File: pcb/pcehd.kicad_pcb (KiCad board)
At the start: 2 copper layers, 118.2 x 73 mm, 163 parts, among them J1 HDMI_CONN, J2 Micro_SD_Card, P1 JTAG_CONN, Q1 BC847, Q2 BC847, U1 AP7361, U10 SN74LVCC4245APW, U11 SN74LVCC4245APW, U12 10CL025YE144C8N, U13 IS25LP016D-JBLE, U14 SN74LVCC4245APW, U15 TLV70012, U16 TLV70025, U17 TLV70012, U18 SN74LVCC4245APW, U19 SN74LVCC4245APW, U2 ADV7513, U20 SN74LVC2G17, U3 TLV70018, U4 PCEngineExpansion, U5 FS7140-01G-XTD, U6 PCM1808PWR, U7 SI5351C-B, U8 74153, U9 SN74LVCC4245APW, Y1 25.000MHz

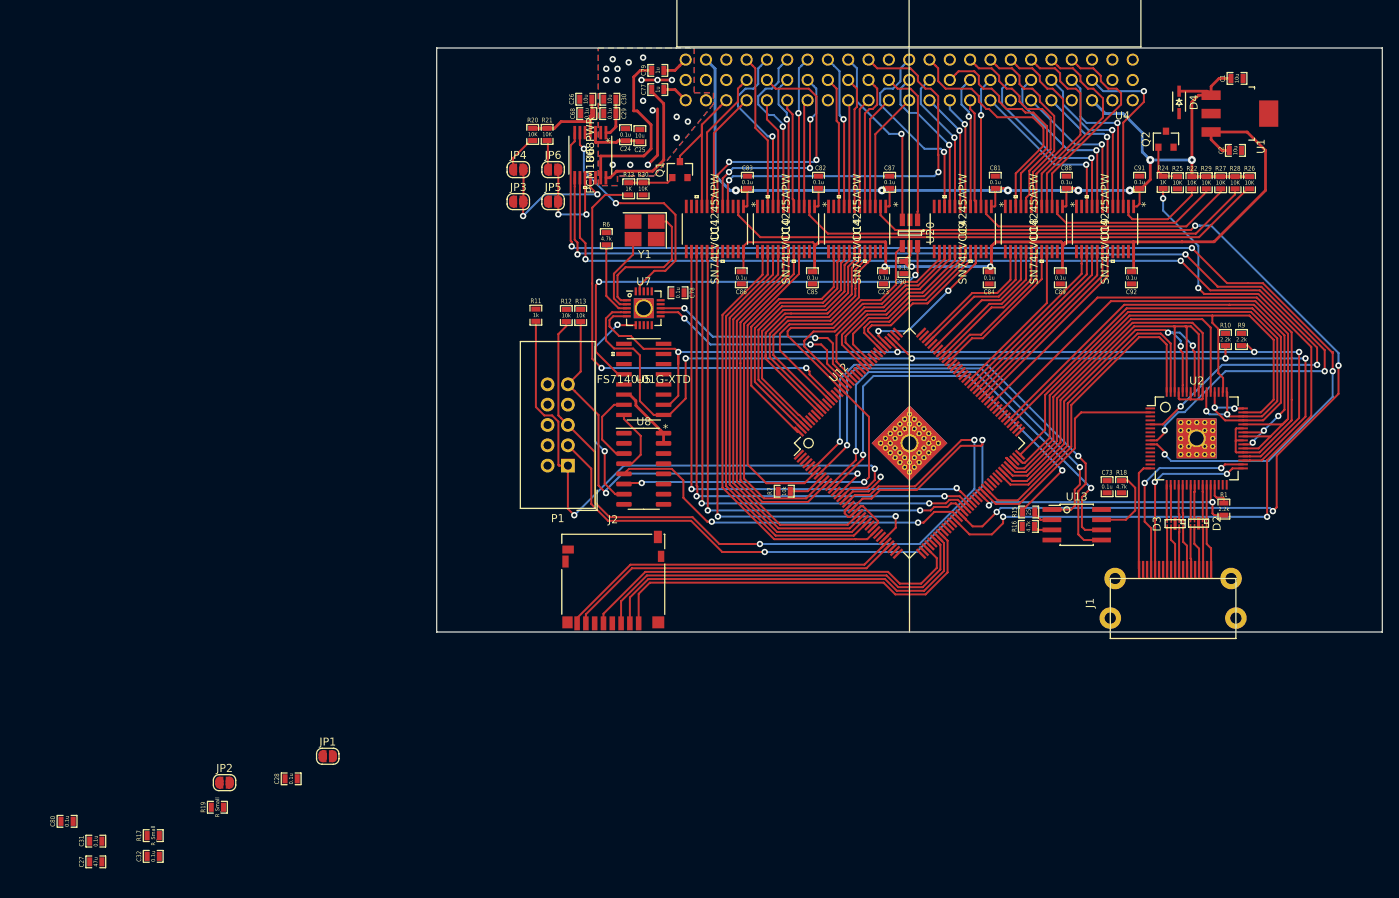
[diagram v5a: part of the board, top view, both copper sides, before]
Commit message: Removed unneeded jumpers
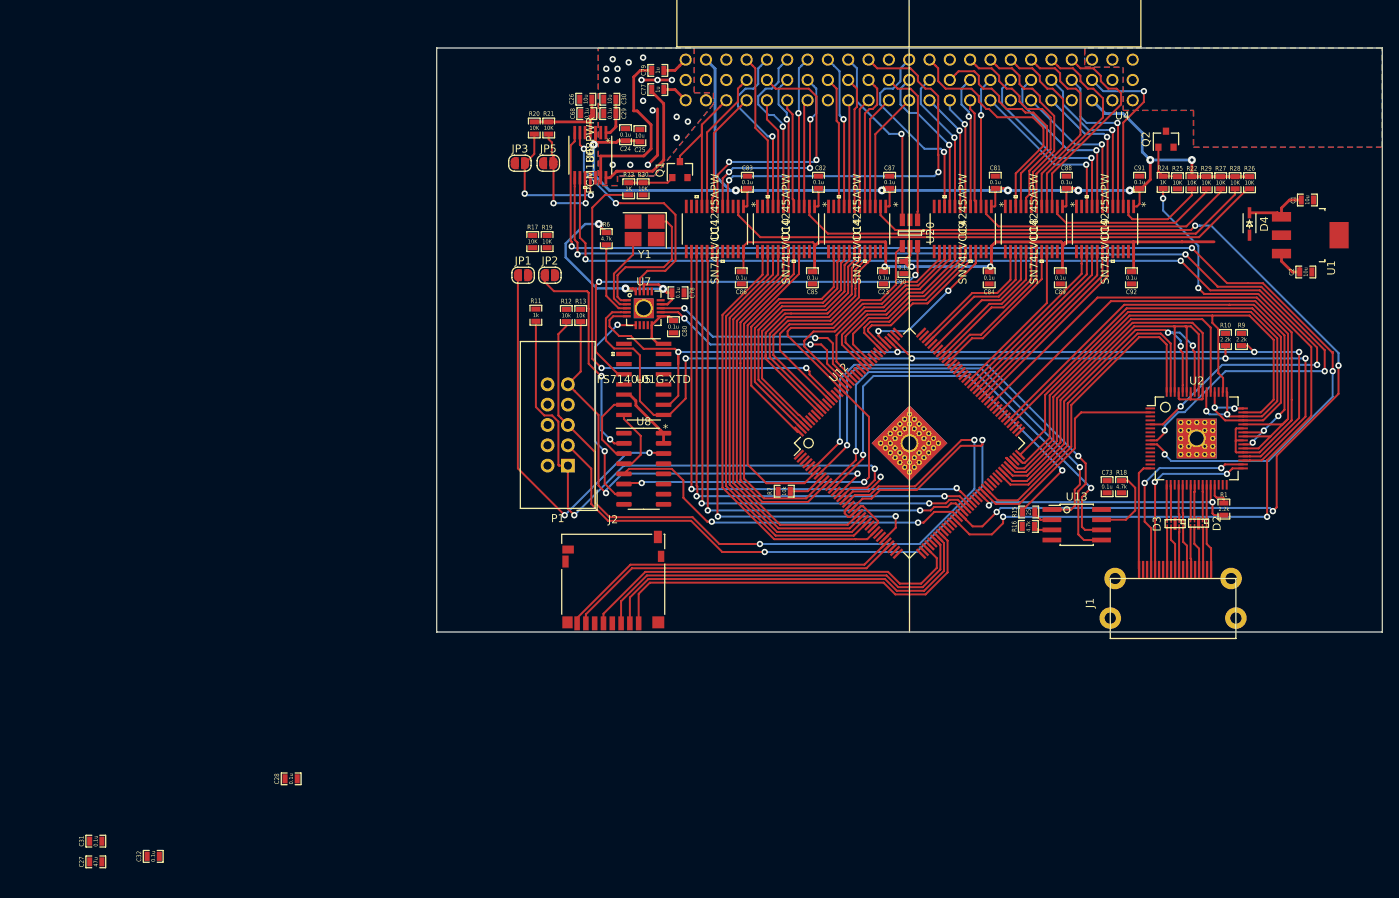
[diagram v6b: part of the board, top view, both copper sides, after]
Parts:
- removed JP4, JP6: SolderJumper_2_Open, Jumper:SolderJumper-2_P1.3mm_Open_RoundedPad1.0x1.5mm
- R17, R19: value R_Small -> 10K
- moved C80 97.8 mm to (101.0, 67.8), turned to 90 degrees
- moved R17 88.1 mm to (83.4, 57.2), turned to 90 degrees
- moved R19 81.8 mm to (85.2, 57.2), turned to 270 degrees
- moved JP2 75.3 mm to (85.5, 61.4)
- moved JP1 64.9 mm to (82.2, 61.4)
- moved C1 17.6 mm to (180.2, 52.0)
- moved C2 17.6 mm to (180.0, 61.0)
- moved D4 17.6 mm to (173.0, 55.0)
- moved U1 17.6 mm to (180.6, 56.4)
- moved JP5 4.84 mm to (85.3, 47.4)
- moved JP3 4.80 mm to (81.8, 47.4)
- moved R21 0.82 mm to (85.4, 43.0)
- moved R20 0.82 mm to (83.6, 43.0)
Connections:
- R20 pad 2: Net-(JP4-Pad1) -> Net-(JP3-Pad2)
- R21 pad 2: Net-(JP6-Pad1) -> Net-(JP5-Pad2)
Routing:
- net Net-(JP1-Pad1): track 0.00 -> 48.0 mm, vias 0 -> 2
- net Net-(JP2-Pad1): track 0.00 -> 28.3 mm, vias 0 -> 2
- net VCC: track 159.8 -> 175.0 mm, vias 4 -> 7
- net /5V: track 147.0 -> 159.7 mm, vias 7 -> 8
- net Net-(JP4-Pad1): track 4.80 -> 0.00 mm
- net Net-(JP6-Pad1): track 3.68 -> 0.00 mm
- net Net-(JP5-Pad2): track 14.1 -> 16.3 mm
- net Net-(U6-Pad6): track 31.0 -> 31.5 mm

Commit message: Layout checkpoint
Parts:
- added C93: 0.1u, custom_components:SM0603_Capa_libcms, F.Cu at (102.1, 80.4)
- added C94: 47u, custom_components:SM0603_Capa_libcms, F.Cu at (107.3, 45.4)
- added C95: 47u, custom_components:SM0603_Capa_libcms, F.Cu at (109.0, 45.3)
- moved C45 214.7 mm to (231.2, 161.5), turned to 90 degrees
- moved C69 211.7 mm to (231.2, 157.9), turned to 90 degrees
- moved C76 206.1 mm to (231.3, 150.7), turned to 90 degrees
- moved C72 201.6 mm to (229.9, 147.1), turned to 90 degrees
- moved U17 201.2 mm to (226.7, 151.3), turned to 90 degrees
- moved C39 201.1 mm to (231.6, 143.5), turned to 90 degrees
- moved C74 198.8 mm to (227.3, 147.4), turned to 90 degrees
- moved C41 198.5 mm to (231.6, 139.9), turned to 90 degrees
- moved C52 196.1 mm to (231.6, 136.3), turned to 90 degrees
- moved C44 195.7 mm to (224.7, 147.4), turned to 90 degrees
- moved C71 195.5 mm to (229.0, 140.2), turned to 90 degrees
- moved C40 193.1 mm to (229.0, 136.7), turned to 90 degrees
- moved C75 192.9 mm to (224.7, 143.8), turned to 90 degrees
- moved C64 191.9 mm to (230.1, 132.8), turned to 90 degrees
- moved C57 189.4 mm to (230.1, 128.8), turned to 90 degrees
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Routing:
- net VCC: track 175.0 -> 211.6 mm, vias 7 -> 9
- net /5V: track 159.7 -> 182.1 mm, vias 8 -> 9
- net /input1/RSTn: track 0.00 -> 11.4 mm
- net Net-(R7-Pad2): track 4.62 -> 14.6 mm, vias 0 -> 2
- net Net-(JP1-Pad1): track 48.0 -> 55.5 mm
- net Net-(U18-Pad5): track 24.6 -> 19.0 mm, vias 0 -> 1
- net Net-(U18-Pad10): track 30.4 -> 24.7 mm
- net Net-(U18-Pad9): track 27.9 -> 23.4 mm
- net Net-(JP2-Pad1): track 28.3 -> 31.9 mm
- net Net-(U18-Pad8): track 26.2 -> 22.8 mm
- net GND: track 8.05 -> 11.5 mm
- net Net-(U19-Pad7): track 18.9 -> 22.2 mm
- net Net-(U18-Pad4): track 25.3 -> 22.0 mm
- net Net-(U19-Pad9): track 23.5 -> 26.8 mm
- net Net-(U19-Pad3): track 22.5 -> 19.4 mm
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
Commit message: Layout near complete
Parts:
- C70, C71, C72, C74, C75, C76, U15, U16, U17: moved to B.Cu
- moved C37 172.9 mm to (38.5, 165.8)
- moved R14 172.9 mm to (38.5, 169.4)
- moved C35 172.9 mm to (46.3, 173.0)
- moved C36 172.9 mm to (43.7, 173.0)
- moved C38 172.9 mm to (41.1, 169.4)
- moved C49 172.9 mm to (46.3, 165.8)
- moved C50 172.9 mm to (56.7, 176.1)
- moved C54 172.9 mm to (51.5, 173.0)
- moved C56 172.9 mm to (43.7, 165.8)
- moved C58 172.9 mm to (46.3, 169.4)
- moved C62 172.9 mm to (48.9, 173.0)
- moved C65 172.9 mm to (43.7, 169.4)
- moved C66 172.9 mm to (41.1, 165.8)
- moved C67 172.9 mm to (48.9, 169.4)
- moved C33 170.5 mm to (55.4, 151.2)
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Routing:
- net VCC: track 211.6 -> 610.5 mm, vias 9 -> 34
- net /fpga1/VCCINT: track 0.00 -> 126.2 mm, vias 0 -> 7
- net /fpga1/VCCA: track 0.00 -> 82.6 mm, vias 0 -> 8
- net /fpga1/VCCD_PLL: track 0.00 -> 77.5 mm, vias 0 -> 7
- net /hdmitx1/DVDD1V8_FILT_DVDD: track 0.00 -> 48.3 mm, vias 0 -> 5
- net /hdmitx1/DVDD1V8_FILT_AVDD: track 0.00 -> 39.6 mm, vias 0 -> 2
- net /hdmitx1/DVDD1V8: track 0.00 -> 39.0 mm, vias 0 -> 2
- net /5V: track 182.1 -> 220.5 mm
- net /hdmitx1/5V_FUSED: track 0.00 -> 17.2 mm, vias 0 -> 2
- net /hdmitx1/DVDD1V8_FILT_PVDD: track 0.00 -> 14.2 mm, vias 0 -> 2
- net Net-(R2-Pad1): track 0.00 -> 12.6 mm, vias 0 -> 2
- net /hdmitx1/DVDD3V3_FILT_DVDD_3V: track 3.23 -> 11.8 mm
- net /hdmitx1/HPD: track 13.8 -> 21.5 mm
- net Net-(D1-Pad1): track 0.00 -> 7.50 mm
- net /fpga1/SCL: track 128.7 -> 135.8 mm
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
